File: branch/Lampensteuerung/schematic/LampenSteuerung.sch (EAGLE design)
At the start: 47 parts, among them IC1 LM358D, IC2 TSOP34836, IC4 TS2951-3.0, Q1 BCR135, Q2 BCR135, Q3 BCR135, Q4 BCW60SMD, T1 SFH320, X2 MKDSN1,5/5-5,08

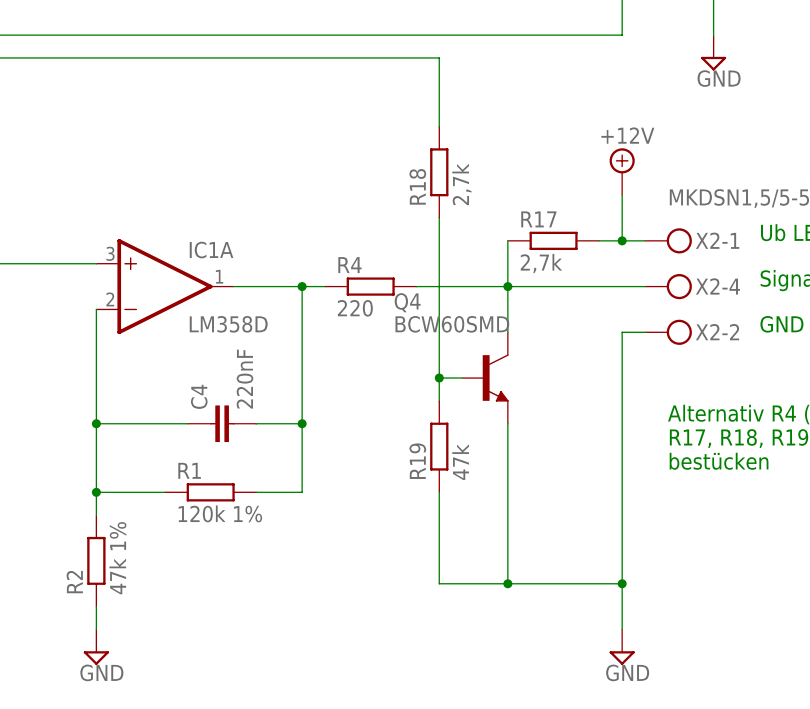
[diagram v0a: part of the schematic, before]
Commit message: added missing pull-up resistors added wire pads for output shifted some components slightly to ease mounting
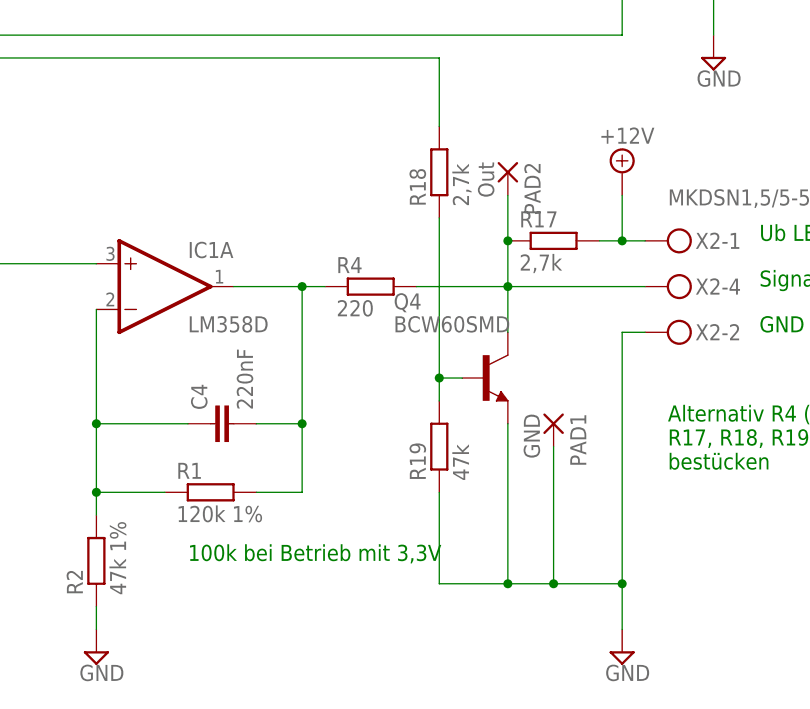
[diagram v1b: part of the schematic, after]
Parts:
- added PAD1: GND, wirepad:1,6/0,8
- added PAD2: Out, wirepad:1,6/0,8
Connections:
- net GND: now also PAD1.P
- net N$9: now also PAD2.P
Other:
- note added: "100k bei Betrieb mit 3,3V"
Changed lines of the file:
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@@
 <part name="R22" library="rcl" deviceset="R-EU_" device="R0805" value="22k"/>
 <part name="SUPPLY5" library="supply2" deviceset="+UB" device=""/>
+<part name="PAD1" library="wirepad" deviceset="1,6/0,8" device="" value="GND"/>
+<part name="PAD2" library="wirepad" deviceset="1,6/0,8" device="" value="Out"/>
 </parts>
 <sheets>
@@
 R17, R18, R19, Q4 (PWM)
 bestücken</text>
+<text x="111.76" y="-38.1" size="1.778" layer="91">100k bei Betrieb mit 3,3V</text>
 </plain>
 <instances>
@@
 <instance part="R22" gate="G$1" x="71.12" y="121.92" rot="R90"/>
 <instance part="SUPPLY5" gate="G$1" x="71.12" y="134.62"/>
+<instance part="PAD1" gate="P" x="152.4" y="-22.86" rot="R270"/>
+<instance part="PAD2" gate="P" x="147.32" y="5.08" rot="R270"/>
 </instances>
 <busses>
@@
 <pinref part="Q4" gate="G$1" pin="E"/>
 <wire x1="147.32" y1="-22.86" x2="147.32" y2="-40.64" width="0.1524" layer="91"/>
-<wire x1="147.32" y1="-40.64" x2="160.02" y2="-40.64" width="0.1524" layer="91"/>
+<wire x1="147.32" y1="-40.64" x2="152.4" y2="-40.64" width="0.1524" layer="91"/>
 <pinref part="R19" gate="G$1" pin="1"/>
+<wire x1="152.4" y1="-40.64" x2="160.02" y2="-40.64" width="0.1524" layer="91"/>
 <wire x1="139.7" y1="-30.48" x2="139.7" y2="-40.64" width="0.1524" layer="91"/>
 <wire x1="139.7" y1="-40.64" x2="147.32" y2="-40.64" width="0.1524" layer="91"/>
 <junction x="147.32" y="-40.64"/>
 <junction x="160.02" y="-40.64"/>
+<pinref part="PAD1" gate="P" pin="P"/>
+<wire x1="152.4" y1="-25.4" x2="152.4" y2="-40.64" width="0.1524" layer="91"/>
+<junction x="152.4" y="-40.64"/>
 </segment>
 <segment>
@@
 <junction x="147.32" y="-7.62"/>
 <wire x1="147.32" y1="-7.62" x2="147.32" y2="-2.54" width="0.1524" layer="91"/>
-</segment>
-</net>
+<pinref part="PAD2" gate="P" pin="P"/>
+<wire x1="147.32" y1="2.54" x2="147.32" y2="-2.54" width="0.1524" layer="91"/>
+<junction x="147.32" y="-2.54"/>
+</segment>
+</net>
